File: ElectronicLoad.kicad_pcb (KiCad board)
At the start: 2 copper layers, 37 parts, among them J1 Load, Q1 MTP3055VL, U1 TLC272, U2 MCP4726A0T, U3 MCP1501-20, U4 INA220

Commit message: USB, MCU
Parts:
- added C10: 100nF, Capacitor_SMD:C_0805_2012Metric_Pad1.18x1.45mm_HandSolder, F.Cu at (33.0, 156.9)
- added C11: 100nF, Capacitor_SMD:C_0805_2012Metric_Pad1.18x1.45mm_HandSolder, F.Cu at (37.8, 153.9)
- added C12: 100nF, Capacitor_SMD:C_0805_2012Metric_Pad1.18x1.45mm_HandSolder, F.Cu at (37.8, 156.9)
- added C14: 100nF, Capacitor_SMD:C_0805_2012Metric_Pad1.18x1.45mm_HandSolder, F.Cu at (69.1, 150.4)
- added C15: 100nF, Capacitor_SMD:C_0805_2012Metric_Pad1.18x1.45mm_HandSolder, F.Cu at (58.4, 139.7)
- added C19: 100nF, Capacitor_SMD:C_0805_2012Metric_Pad1.18x1.45mm_HandSolder, F.Cu at (61.0, 127.5)
- added C3: 18pF, Capacitor_SMD:C_0805_2012Metric_Pad1.18x1.45mm_HandSolder, F.Cu at (60.5, 159.5)
- added C4: 18pF, Capacitor_SMD:C_0805_2012Metric_Pad1.18x1.45mm_HandSolder, F.Cu at (65.5, 159.5)
- added C6: 1μF, Capacitor_SMD:C_0805_2012Metric_Pad1.18x1.45mm_HandSolder, F.Cu at (49.8, 147.8)
- added C9: 10μF, Capacitor_Tantalum_SMD:CP_EIA-3216-18_Kemet-A_Pad1.58x1.35mm_HandSolder, F.Cu at (39.1, 124.0)
- added D1: TX, LED_SMD:LED_0805_2012Metric_Pad1.15x1.40mm_HandSolder, F.Cu at (44.7, 176.8)
- added D2: RX, LED_SMD:LED_0805_2012Metric_Pad1.15x1.40mm_HandSolder, F.Cu at (47.2, 176.8)
- added D3: VCC, LED_SMD:LED_0805_2012Metric_Pad1.15x1.40mm_HandSolder, F.Cu at (49.8, 176.8)
- added D4: SK520BTR, Diode_SMD:D_SMB, F.Cu at (114.8, 166.1)
- added D5: L4148, Diode_SMD:D_MiniMELF, F.Cu at (61.0, 131.1)
- added F1: 500mA, Fuse:Fuse_1812_4532Metric_Pad1.30x3.40mm_HandSolder, F.Cu at (84.8, 152.4)
- added F2: 5A Fast, Fuse:Fuse_1206_3216Metric_Pad1.42x1.75mm_HandSolder, F.Cu at (120.9, 166.1)
- added H1: TagConnect, Connector:Tag-Connect_TC2030-IDC-NL_2x03_P1.27mm_Vertical, F.Cu at (82.3, 131.6)
- added H2: ICSP, Connector_PinHeader_2.54mm:PinHeader_2x03_P2.54mm_Vertical, F.Cu at (74.2, 129.0)
- added J1: USB_B, DTLib:USB_B_OST_USB-B1HSxx_Horizontal, F.Cu at (87.4, 168.7)
- added L1: Ferrite, Inductor_SMD:L_0805_2012Metric_Pad1.15x1.40mm_HandSolder, F.Cu at (77.4, 143.3)
- added L2: 10μH, Inductor_SMD:L_0805_2012Metric_Pad1.15x1.40mm_HandSolder, F.Cu at (69.1, 152.4)
- added L3: 10μH, Inductor_SMD:L_0805_2012Metric_Pad1.15x1.40mm_HandSolder, F.Cu at (55.9, 139.7)
- added R1: 22R, Resistor_SMD:R_0805_2012Metric_Pad1.20x1.40mm_HandSolder, F.Cu at (84.1, 144.2)
- added R2: 22R, Resistor_SMD:R_0805_2012Metric_Pad1.20x1.40mm_HandSolder, F.Cu at (76.6, 148.4)
- added R28: 330R, Resistor_SMD:R_0805_2012Metric_Pad1.20x1.40mm_HandSolder, F.Cu at (66.5, 131.1)
- added R29: 4.7K, Resistor_SMD:R_0805_2012Metric_Pad1.20x1.40mm_HandSolder, F.Cu at (66.5, 128.0)
- added R3: 100R, Resistor_SMD:R_0805_2012Metric_Pad1.20x1.40mm_HandSolder, F.Cu at (84.1, 147.1)
- added R4: 10K, Resistor_SMD:R_0805_2012Metric_Pad1.20x1.40mm_HandSolder, F.Cu at (66.5, 166.1)
- added R5: 10K, Resistor_SMD:R_0805_2012Metric_Pad1.20x1.40mm_HandSolder, F.Cu at (61.8, 166.1)
- added RN1: 1K, Resistor_SMD:R_Array_Convex_4x1206, F.Cu at (47.2, 171.7)
- added RV1: MOV-07D330K, Varistor:RV_Disc_D9mm_W3.4mm_P5mm, F.Cu at (114.3, 158.0)
- added SW1: RESET, Button_Switch_SMD:SW_Push_1P1T_NO_6x6mm_H9.5mm, F.Cu at (64.0, 119.9)
- added U2: ATmega32U4-AU, Package_QFP:TQFP-44_10x10mm_P0.8mm, F.Cu at (59.7, 149.1)
- added U6: NUP2114, Package_TO_SOT_SMD:TSOT-23-6, F.Cu at (86.4, 163.1)
- added Y1: 16MHz, Crystal:Crystal_HC49-4H_Vertical, F.Cu at (64.0, 174.2)
- moved C8 42.4 mm to (33.0, 124.0)
- moved R10 33.8 mm to (46.2, 127.0)
- moved C16 33.8 mm to (42.2, 128.5)
- moved R11 33.8 mm to (46.2, 129.5)
- moved U5 33.6 mm to (36.1, 129.0)
- moved J2 33.2 mm to (113.8, 176.3)
- moved C18 21.6 mm to (96.5, 125.5)
- moved R25 21.1 mm to (96.5, 129.0), turned to 180 degrees
- moved U4 7.64 mm to (79.8, 109.6)
- moved Q1 5.40 mm to (101.6, 138.2)
- moved C5 3.09 mm to (73.2, 109.2), turned to 90 degrees
- moved C2 1.88 mm to (75.7, 109.7), turned to 90 degrees
- renumbered C3 to C1, C6 to C13, C9 to C16, C1 to C17, C2 to C18, C4 to C2, J1 to J2, R21 to R10, R22 to R11, R20 to R12, R1 to R13, R2 to R14, R3 to R15, R4 to R16, R5 to R17, R6 to R18, R7 to R19, R11 to R20, R8 to R21, R12 to R22, R9 to R23, R10 to R24, R15 to R25, R13 to R26, R14 to R27, R16 to R6, R17 to R7, R18 to R8, R19 to R9, U2 to U4, U4 to U5
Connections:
- Q1 pad 2: VLOAD -> Net-(F2-Pad2)
- R25 pad 1: VLOAD -> Net-(F2-Pad2)
- U4 pad 2: SCL -> GND
- U4 pad 5: (no net) -> SCL

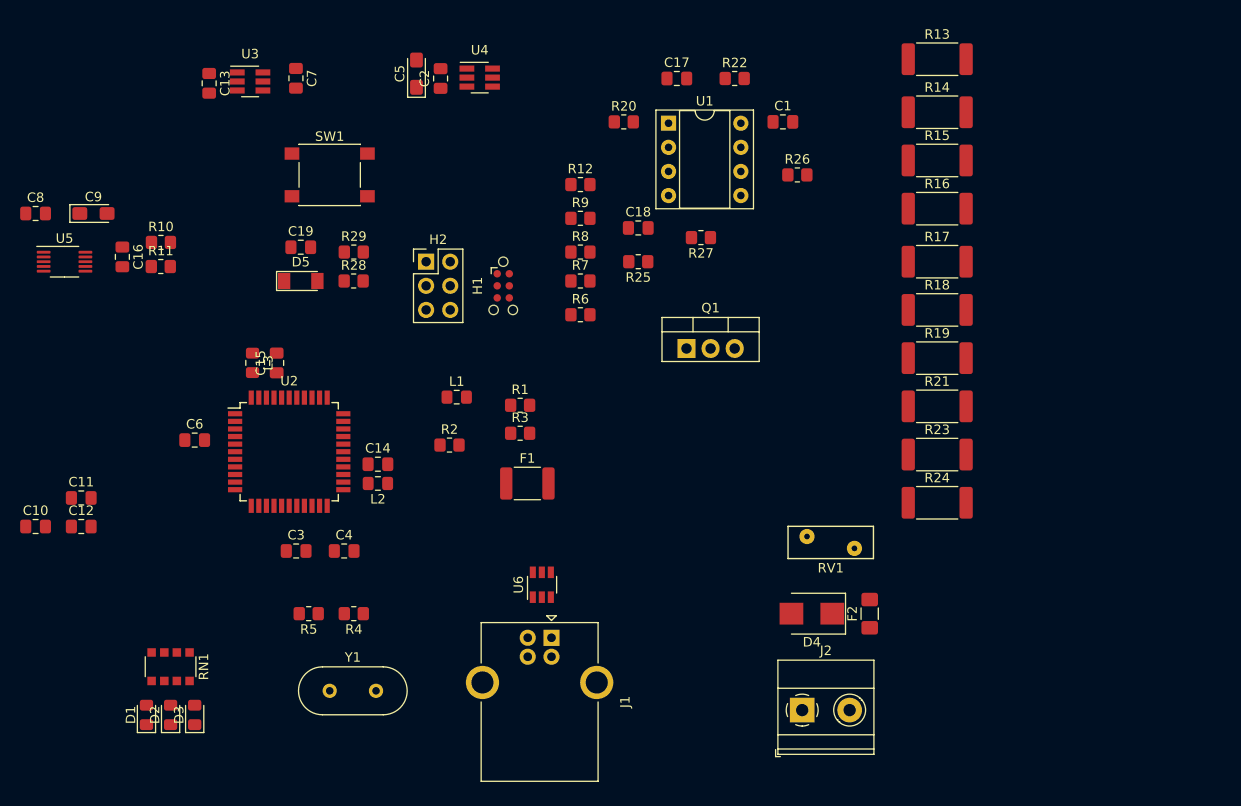
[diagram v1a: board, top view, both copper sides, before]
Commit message: Fan control
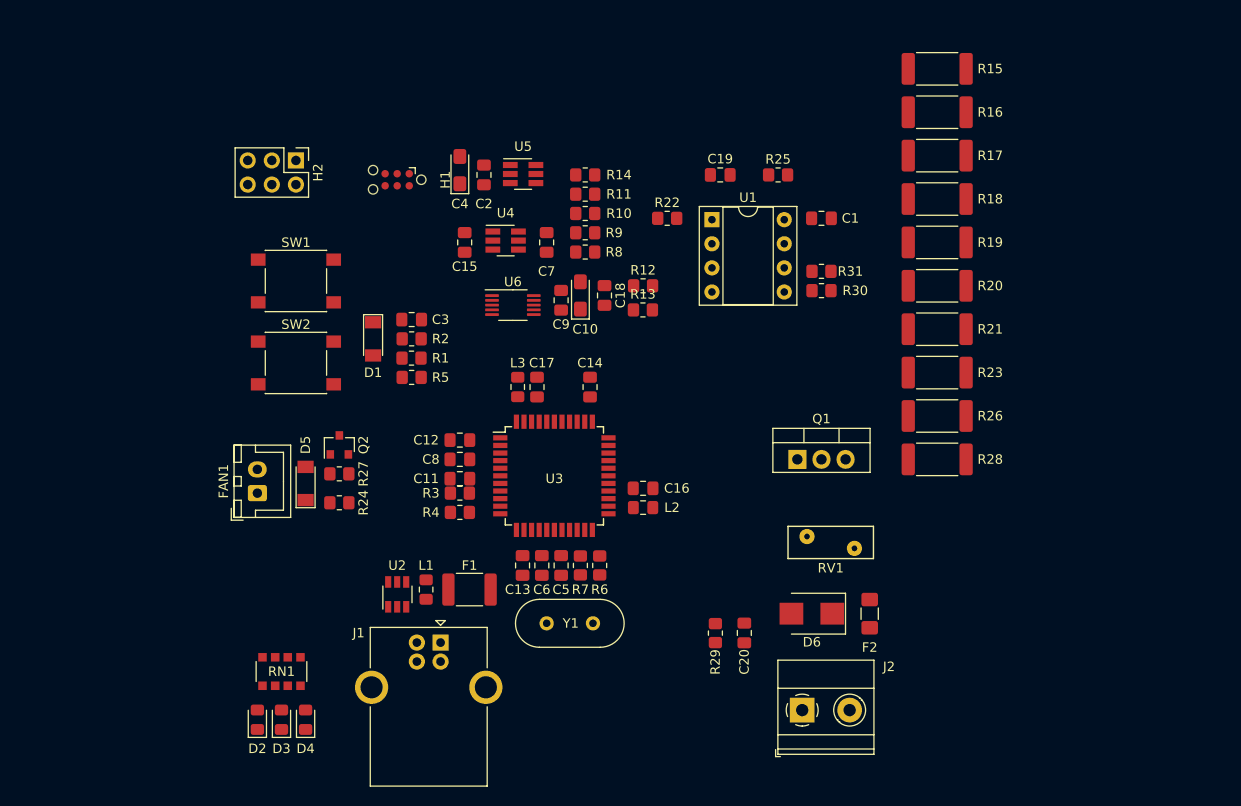
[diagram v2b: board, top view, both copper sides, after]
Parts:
- removed the C5 at (73.2, 109.2)
- removed the R3 at (84.1, 147.1)
- added C14: 100nF, Capacitor_SMD:C_0805_2012Metric_Pad1.18x1.45mm_HandSolder, F.Cu at (91.4, 142.2)
- added C4: 10μF, Capacitor_Tantalum_SMD:CP_EIA-3216-18_Kemet-A_Pad1.58x1.35mm_HandSolder, F.Cu at (77.7, 119.4)
- added D5: L4148, Diode_SMD:D_MiniMELF, F.Cu at (61.5, 152.4)
- added FAN1: 5V, Connector_JST:JST_XH_B2B-XH-A_1x02_P2.50mm_Vertical, F.Cu at (56.4, 153.4)
- added Q2: DMG2302U, Package_TO_SOT_SMD:SOT-23, F.Cu at (65.0, 148.3)
- added R24: 100R, Resistor_SMD:R_0805_2012Metric_Pad1.20x1.40mm_HandSolder, F.Cu at (65.0, 154.4)
- added R27: 10K, Resistor_SMD:R_0805_2012Metric_Pad1.20x1.40mm_HandSolder, F.Cu at (65.0, 151.4)
- added R5: 10K, Resistor_SMD:R_0805_2012Metric_Pad1.20x1.40mm_HandSolder, F.Cu at (72.6, 141.2)
- added SW2: BOOTLOADER, Button_Switch_SMD:SW_Push_1P1T_NO_6x6mm_H9.5mm, F.Cu at (60.5, 139.7)
- moved C9 56.1 mm to (88.4, 133.1), turned to 90 degrees
- moved C10 52.0 mm to (90.4, 132.6), turned to 90 degrees
- moved R12 51.0 mm to (97.0, 131.6)
- moved R13 51.0 mm to (97.0, 134.1)
- moved C18 51.0 mm to (93.0, 132.6)
- moved U6 47.5 mm to (83.3, 133.6)
- moved C13 46.7 mm to (84.3, 161.0), turned to 270 degrees
- moved C11 45.0 mm to (77.7, 151.9), turned to 180 degrees
- moved C20 44.1 mm to (107.7, 168.1), turned to 270 degrees
- moved C12 40.4 mm to (77.7, 147.8), turned to 180 degrees
- moved R29 40.0 mm to (104.6, 168.2), turned to 90 degrees
- moved U4 31.7 mm to (82.5, 126.8)
- moved C15 31.7 mm to (78.2, 127.0)
- moved C7 31.6 mm to (86.9, 127.0)
- moved R7 29.1 mm to (90.4, 161.0), turned to 90 degrees
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- renumbered C9 to C10, C10 to C11, C11 to C12, C12 to C13, C13 to C15, C14 to C16, C15 to C17, C16 to C18, C17 to C19, C18 to C20, C19 to C3, C3 to C5, C4 to C6, C6 to C8, C8 to C9, D5 to D1, D1 to D2, D2 to D3, D3 to D4, D4 to D6, R28 to R1, R8 to R10, R9 to R11, R10 to R12, R11 to R13, R12 to R14, R13 to R15, R14 to R16, R15 to R17, R16 to R18, R17 to R19, R29 to R2, R18 to R20, R19 to R21, R20 to R22, R21 to R23, R22 to R25, R23 to R26, R24 to R28, R25 to R29, R1 to R3, R26 to R30, R27 to R31, R2 to R4, R4 to R6, R5 to R7, R6 to R8, R7 to R9, U6 to U2, U2 to U3, U3 to U4, U4 to U5, U5 to U6
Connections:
- net Net-(C3-Pad2) renamed /XTAL1
- net Net-(C4-Pad2) renamed /XTAL2
- U3 pad 33: Net-(R3-Pad1) -> /~HWB

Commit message: Power switch, led
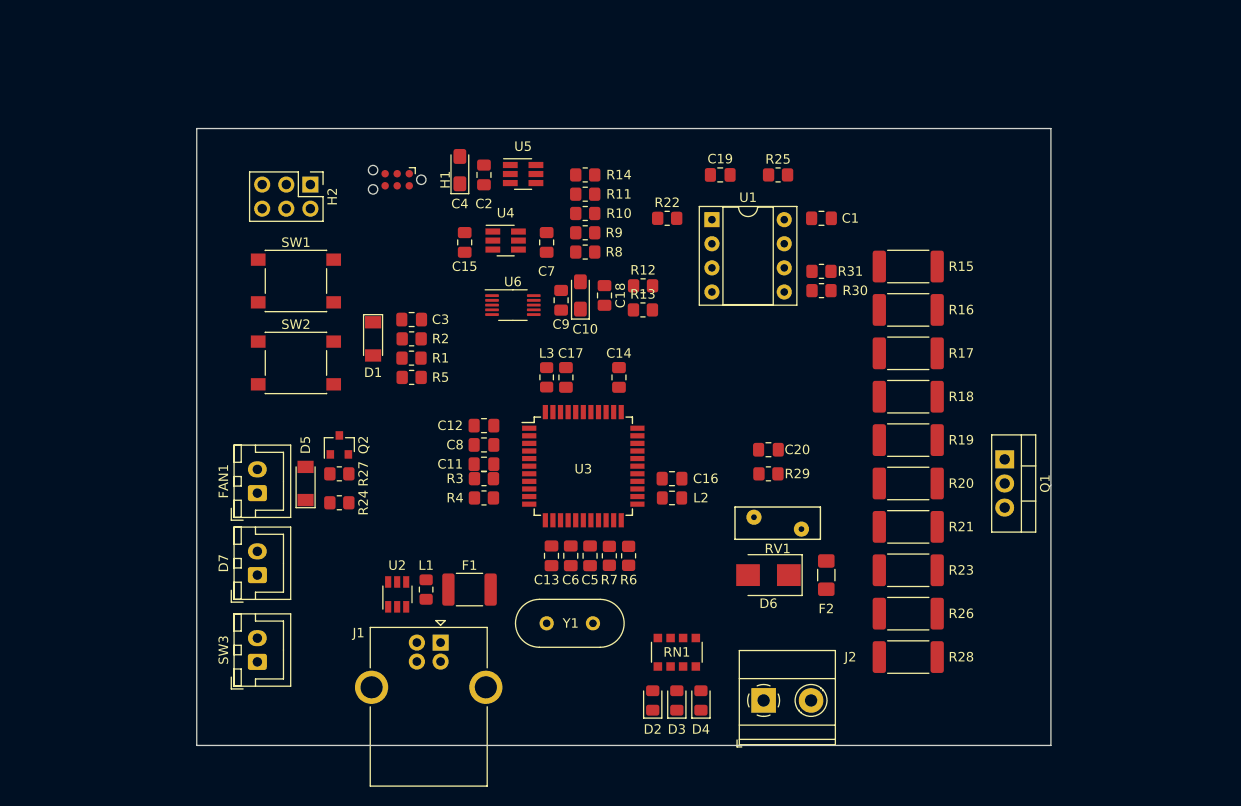
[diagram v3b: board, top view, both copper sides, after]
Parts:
- added D7: POWER-CASE, Connector_JST:JST_XH_B2B-XH-A_1x02_P2.50mm_Vertical, F.Cu at (56.4, 162.1)
- added SW3: POWER, Connector_JST:JST_XH_B2B-XH-A_1x02_P2.50mm_Vertical, F.Cu at (56.4, 171.2)
- D4: value VCC -> POWER
- moved D3 41.7 mm to (100.6, 175.3)
- moved RN1 41.7 mm to (100.6, 170.2)
- moved D2 41.7 mm to (98.0, 175.3)
- moved D4 41.7 mm to (103.1, 175.3)
- moved Q1 21.8 mm to (135.1, 149.9), turned to 270 degrees
- moved R17 21.0 mm to (125.0, 138.7)
- moved R18 21.0 mm to (125.0, 143.3)
- moved R19 21.0 mm to (125.0, 147.8)
- moved R20 21.0 mm to (125.0, 152.4)
- moved R21 21.0 mm to (125.0, 157.0)
- moved R23 21.0 mm to (125.0, 161.5)
- moved R26 21.0 mm to (125.0, 166.1)
- moved R15 21.0 mm to (125.0, 129.5)
- moved R16 21.0 mm to (125.0, 134.1)
- moved R28 21.0 mm to (125.0, 170.7)
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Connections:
- L1 pad 1: /VBUS -> /VSW
- RN1 pad 2: RXLED -> VCC
- RN1 pad 3: TXLED -> RXLED
- RN1 pad 4: Net-(RN1-Pad4) -> TXLED
- RN1 pad 5: Net-(RN1-Pad5) -> Net-(D2-Pad2)
- RN1 pad 6: Net-(D2-Pad2) -> Net-(D3-Pad2)
- RN1 pad 7: Net-(D3-Pad2) -> Net-(D4-Pad2)
- RN1 pad 8: Net-(D4-Pad2) -> Net-(D7-Pad2)
- U2 pad 5: /VBUS -> /VSW
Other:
- board outline added: 90 x 65 mm

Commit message: Encoder, layout
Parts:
- removed R30, R31, R6, R7: 10K, Resistor_SMD:R_0805_2012Metric_Pad1.20x1.40mm_HandSolder
- added C11: 100nF, Capacitor_SMD:C_0805_2012Metric_Pad1.18x1.45mm_HandSolder, F.Cu at (134.1, 129.5)
- added C12: 10μF, Capacitor_Tantalum_SMD:CP_EIA-3216-18_Kemet-A_Pad1.58x1.35mm_HandSolder, F.Cu at (76.2, 158.0)
- added C23: 10nF, Capacitor_SMD:C_0805_2012Metric_Pad1.18x1.45mm_HandSolder, F.Cu at (79.8, 130.6)
- added C24: 10nF, Capacitor_SMD:C_0805_2012Metric_Pad1.18x1.45mm_HandSolder, F.Cu at (79.8, 132.6)
- added C25: 10nF, Capacitor_SMD:C_0805_2012Metric_Pad1.18x1.45mm_HandSolder, F.Cu at (79.8, 128.5)
- added H1: MountingHole_Pad, MountingHole:MountingHole_3.2mm_M3_ISO7380_Pad, F.Cu at (55.0, 120.0)
- added H2: MountingHole_Pad, MountingHole:MountingHole_3.2mm_M3_ISO7380_Pad, F.Cu at (135.0, 120.0)
- added H3: MountingHole_Pad, MountingHole:MountingHole_3.2mm_M3_ISO7380_Pad, F.Cu at (135.0, 175.0)
- added H4: MountingHole_Pad, MountingHole:MountingHole_3.2mm_M3_ISO7380_Pad, F.Cu at (55.0, 175.0)
- added J3: CONN_A, Connector_JST:JST_XH_B6B-XH-A_1x06_P2.50mm_Vertical, F.Cu at (66.5, 131.6)
- added LCD1: LCD_2X12-I2C, Connector_JST:JST_XH_B4B-XH-A_1x04_P2.50mm_Vertical, F.Cu at (92.5, 174.8)
- added RN2: 10K, Resistor_SMD:R_Array_Convex_4x1206, F.Cu at (75.1, 130.9)
- added RN3: 10K, Resistor_SMD:R_Array_Convex_4x1206, F.Cu at (94.5, 160.5)
- added SW4: Control, DTLib:RotaryEncoder_Bourns_PEC16-2xxxF-Sxxxx, F.Cu at (55.9, 135.1)
- added U7: PCT2075D, Package_SO:SO-8_3.9x4.9mm_P1.27mm, F.Cu at (135.1, 134.6)
- D2: renamed from D6; value SK520BTR -> S10ML-TP; footprint Diode_SMD:D_SMB -> Diode_SMD:D_SMC
- F2: value 5A Fast -> 10A Fast 1206
- RV1: value MOV-07D330K -> VC0805K121R020; footprint Varistor:RV_Disc_D9mm_W3.4mm_P5mm -> Resistor_SMD:R_0805_2012Metric_Pad1.20x1.40mm_HandSolder
- SW2: renamed from SW1; footprint Button_Switch_SMD:SW_Push_1P1T_NO_6x6mm_H9.5mm -> Button_Switch_SMD:SW_SPST_PTS645
- SW3: renamed from SW2; footprint Button_Switch_SMD:SW_Push_1P1T_NO_6x6mm_H9.5mm -> Button_Switch_SMD:SW_SPST_PTS645
- U1: footprint Package_DIP:DIP-8_W7.62mm_Socket -> Package_DIP:DIP-8_W7.62mm_Socket_LongPads
- U5: value MCP4726A0T -> MCP4726A3T
- moved R26 37.2 mm to (115.8, 134.6), turned to 180 degrees
- moved C10 36.1 mm to (107.2, 164.6), turned to 180 degrees
- moved C9 35.2 mm to (107.7, 162.6), turned to 180 degrees
- moved U6 34.9 mm to (106.7, 159.5)
- moved J5 34.6 mm to (96.5, 118.4)
- moved C20 33.4 mm to (112.8, 159.5)
- moved C4 33.2 mm to (107.7, 133.6)
- moved R12 33.1 mm to (116.3, 158.5)
- moved R13 32.7 mm to (116.3, 160.5)
- moved C14 31.2 mm to (106.7, 139.7), turned to 180 degrees
- moved SW3 30.4 mm to (84.3, 120.9), turned to 270 degrees
- moved U4 29.5 mm to (106.9, 143.5), turned to 270 degrees
- moved R14 29.4 mm to (101.6, 147.3), turned to 180 degrees
- moved C2 28.7 mm to (105.2, 134.1)
- moved R25 28.4 mm to (115.8, 139.2), turned to 180 degrees
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- renumbered C11 to C13, C15 to C14, C12 to C15, C13 to C16, C14 to C17, C16 to C18, C17 to C19, C18 to C20, C19 to C21, C20 to C22, D5 to D3, H1 to J4, H2 to J5, D2 to LED1, D3 to LED2, D4 to LED3, D7 to LED4, R25 to R24, R26 to R25, R28 to R26, R29 to R27, R24 to R28, R27 to R29, SW3 to SW1
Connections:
- net Net-(Q1-Pad1) renamed ~OT_SHUTDOWN
- D2 pad 1: Net-(D6-Pad1) -> Net-(D2-Pad1)
- D2 pad 2: VLOAD -> GND
- F2 pad 1: Net-(D6-Pad1) -> VLOAD
- F2 pad 2: Net-(F2-Pad2) -> Net-(D2-Pad1)
- J2 pad 1: VLOAD -> GND
- J2 pad 2: GND -> VLOAD
- LED1 pad 1: GND -> ~TXLED
- LED2 pad 1: GND -> ~RXLED
- Q1 pad 2: Net-(F2-Pad2) -> Net-(D2-Pad1)
- R10 pad 1: /ISET_DIV5 -> GND
- R10 pad 2: GND -> /ISET_DIV5
- R11 pad 1: /ISET_DIV5 -> GND
- R11 pad 2: GND -> /ISET_DIV5
- R14 pad 1: /ISET_DIV5 -> GND
- R14 pad 2: GND -> /ISET_DIV5
- R27 pad 1: Net-(F2-Pad2) -> Net-(D2-Pad1)
- RN1 pad 3: RXLED -> VCC
- RN1 pad 4: TXLED -> VCC
- RV1 pad 1: Net-(F2-Pad2) -> Net-(D2-Pad1)
- U1 pad 5: Net-(R30-Pad2) -> /ILOAD+
- U1 pad 6: Net-(U1-Pad6) -> ILOAD_MCU
- U1 pad 7: Net-(U1-Pad6) -> ILOAD_MCU
- U3 pad 1: /D7 -> ROT_SW
- U3 pad 12: /D11 -> FAN_PWM
- U3 pad 20: /D0|RX -> ROT_A
- U3 pad 21: /D1|TX -> ROT_B
- U3 pad 22: TXLED -> ~TXLED
- U3 pad 36: /A0 -> ILOAD_MCU
- U3 pad 8: RXLED -> ~RXLED

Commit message: Heatsink, Fan, Layout
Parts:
- removed SW1: POWER, Connector_JST:JST_XH_B2B-XH-A_1x02_P2.50mm_Vertical
- added C26: 100nF, Capacitor_SMD:C_0805_2012Metric_Pad1.18x1.45mm_HandSolder, F.Cu at (135.1, 151.4)
- added C27: 1μF, Capacitor_SMD:C_0805_2012Metric_Pad1.18x1.45mm_HandSolder, F.Cu at (67.1, 128.0)
- added HS1: Heatsink, DTLib:HSINK_6396BG, F.Cu at (145.3, 147.3)
- added R6: 1R, Resistor_SMD:R_0805_2012Metric_Pad1.20x1.40mm_HandSolder, F.Cu at (64.5, 128.0)
- added U8: PCT2075D, Package_SO:SO-8_3.9x4.9mm_P1.27mm, F.Cu at (136.7, 156.0)
- D2: value S10ML-TP -> SK520BTR; footprint Diode_SMD:D_SMC -> Diode_SMD:D_SMB_Handsoldering
- F2: value 10A Fast 1206 -> 5A Fast; footprint Fuse:Fuse_1206_3216Metric_Pad1.42x1.75mm_HandSolder -> DTLib:Fuse_PTF-76
- J3: value CONN_A -> AUX1; footprint Connector_JST:JST_XH_B6B-XH-A_1x06_P2.50mm_Vertical -> Connector_PinHeader_2.54mm:PinHeader_1x06_P2.54mm_Vertical
- LCD1: value LCD_2X12-I2C -> LCD_2X16-I2C
- moved J3 26.4 mm to (89.9, 119.4), turned to 0 degrees
- moved R15 25.4 mm to (124.5, 160.0), turned to 180 degrees
- moved FAN1 22.9 mm to (67.1, 117.9), turned to 0 degrees
- moved J2 20.8 mm to (130.6, 174.2)
- moved C24 20.0 mm to (63.5, 144.3), turned to 270 degrees
- moved C25 19.9 mm to (67.6, 144.3), turned to 270 degrees
- moved C23 19.8 mm to (65.5, 144.3), turned to 270 degrees
- moved R21 18.0 mm to (124.5, 132.6)
- moved R20 18.0 mm to (124.5, 137.2)
- moved D1 17.7 mm to (76.7, 139.2), turned to 270 degrees
- moved D2 17.6 mm to (110.9, 165.6), turned to 0 degrees
- moved R23 17.5 mm to (124.5, 128.5)
- moved D3 17.3 mm to (66.0, 124.5), turned to 0 degrees
- moved R25 17.1 mm to (124.5, 124.5)
- moved R26 16.6 mm to (124.5, 120.4)
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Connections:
- net /D+AVR renamed /D_AVR+
- net /D+USB renamed /D_USB+
- net /D-AVR renamed /D_AVR-
- net /D-USB renamed /D_USB-
- net Net-(C20-Pad1) renamed /Vin+
- net Net-(C20-Pad2) renamed /Vin-
- net Net-(D3-Pad2) renamed /FAN-
- D2 pad 1: Net-(D2-Pad1) -> VLOAD
- D3 pad 1: VCC -> FAN_VCC
- F2 pad 1: VLOAD -> /LOAD
- F2 pad 2: Net-(D2-Pad1) -> VLOAD
- FAN1 pad 1: VCC -> FAN_VCC
- J2 pad 2: VLOAD -> /LOAD
- L1 pad 1: /VSW -> /VBUS
- Q1 pad 2: Net-(D2-Pad1) -> VLOAD
- R27 pad 1: Net-(D2-Pad1) -> VLOAD
- RV1 pad 1: Net-(D2-Pad1) -> VLOAD
- U2 pad 5: /VSW -> /VBUS
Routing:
- net GND: track 0.00 -> 88.9 mm, vias 0 -> 18
- net VCC: track 0.00 -> 63.0 mm, vias 0 -> 12
- net ILOAD_MCU: track 0.00 -> 35.5 mm
- net VREF2048: track 0.00 -> 34.2 mm
- net /D_USB+: track 0.00 -> 27.1 mm
- net /D_USB-: track 0.00 -> 23.4 mm
- net Net-(RN2-Pad1): track 0.00 -> 18.1 mm
- net /ISET_DIV5: track 0.00 -> 13.0 mm
- net Net-(RN2-Pad3): track 0.00 -> 12.9 mm
- net /Vin-: track 0.00 -> 12.7 mm
- net FAN_VCC: track 0.00 -> 12.4 mm
- net /FAN-: track 0.00 -> 9.37 mm
- net /Vin+: track 0.00 -> 8.86 mm
- net AVCC: track 0.00 -> 6.98 mm
- net /~RESET: track 0.00 -> 6.92 mm
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- added copper zone on In1.Cu, net GND
- added copper zone on In2.Cu, net VCC
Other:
- board size 90 x 65 mm -> 100 x 65 mm
- copper layers 2 -> 4
- net class LOAD added: clearance 0.2, trace_width 1, via_dia 1, via_drill 0.4
- net class POWER added: clearance 0.2, trace_width 0.5, via_dia 0.8, via_drill 0.4

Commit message: Routing
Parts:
- D2: footprint Diode_SMD:D_SMB_Handsoldering -> Diode_SMD:D_SMB
- moved R15 3.05 mm to (124.5, 157.0)
- moved R16 2.54 mm to (124.5, 152.9)
- moved R17 2.03 mm to (124.5, 148.8)
- moved R18 1.52 mm to (124.5, 144.8)
- moved R19 1.02 mm to (124.5, 140.7)
- moved R20 0.51 mm to (124.5, 136.7)
- moved R22 0.51 mm to (115.8, 118.4)
- moved C16 0.25 mm to (85.3, 160.3)
- moved C21 0.25 mm to (115.8, 120.7)
- moved C5 0.25 mm to (85.3, 164.8)
- turned D2 to 180 degrees
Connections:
- J2 pad 1: GND -> /LOAD
- J2 pad 2: /LOAD -> GND
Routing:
- net GND: track 88.9 -> 249.1 mm, vias 18 -> 84
- net SDA: track 5.54 -> 123.9 mm, vias 0 -> 5
- net SCL: track 4.10 -> 121.2 mm, vias 0 -> 4
- net VLOAD: track 0.00 -> 103.9 mm
- net /ILOAD+: track 0.00 -> 97.0 mm
- net ROT_SW: track 0.00 -> 83.5 mm, vias 0 -> 2
- net VCC: track 63.0 -> 128.7 mm, vias 12 -> 30
- net /MISO: track 0.00 -> 65.0 mm, vias 0 -> 1
- net Net-(RN3-Pad3): track 0.00 -> 64.5 mm, vias 0 -> 1
- net /MOSI: track 0.00 -> 64.3 mm, vias 0 -> 2
- net ~OT_SHUTDOWN: track 0.00 -> 64.2 mm, vias 0 -> 1
- net /SCK: track 0.00 -> 58.6 mm, vias 0 -> 1
- net ~RXLED: track 0.00 -> 57.5 mm, vias 0 -> 2
- net ~EXT_RESET: track 0.00 -> 46.5 mm
- net Net-(LED4-Pad2): track 0.00 -> 42.8 mm, vias 0 -> 1
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- added copper zone on B.Cu, net GND
- added copper zone on F.Cu, net GND
- added copper zone on F.Cu, net VCC
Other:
- outline, holes or cut-outs redrawn
- rule via_min_size: 0.4 -> 0.6
